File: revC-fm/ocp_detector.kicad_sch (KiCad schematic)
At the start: 13 parts, among them Q5 MMDT3946, Q59 BSZ180, U34 INA300AIDSQT

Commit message: updated fab files
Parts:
- C146: Manufacturer (none) -> TDK; Mfr. Part No (none) -> CGA2B3X7R1H104K050BE
- C71: renamed from C111; Manufacturer (none) -> TDK; Mfr. Part No (none) -> CGA3E1X7R1V105K080AE
- D8: renamed from D20; Manufacturer (none) -> onsemi; Mfr. Part No (none) -> 1SS400T1G
- Q5: Manufacturer (none) -> Diodes Incorporated
- Q59: Manufacturer (none) -> Infineon
- R129: renamed from R224; Manufacturer (none) -> Panasonic; Mfr. Part No (none) -> ERJ-2GEJ102X
- R130: renamed from R223; Manufacturer (none) -> Stackpole Electronics; Mfr. Part No (none) -> RMCF0402FT100K
- R131: renamed from R221; Manufacturer (none) -> Stackpole Electronics; Mfr. Part No (none) -> RMCF0402FT10K0
- R132: renamed from R225; Manufacturer (none) -> Stackpole Electronics; Mfr. Part No (none) -> RMCF0402FT100K
- R133: renamed from R222; Manufacturer (none) -> Panasonic; Mfr. Part No (none) -> ERJ-2GEJ102X
- R36: Manufacturer (none) -> Vishay Dale; Mfr. Part No WSLPx -> WSLP1206R0220
- RN5: renamed from RN7; Manufacturer (none) -> Stackpole Electronics
- U18: renamed from U34; Manufacturer (none) -> Vishay Siliconix

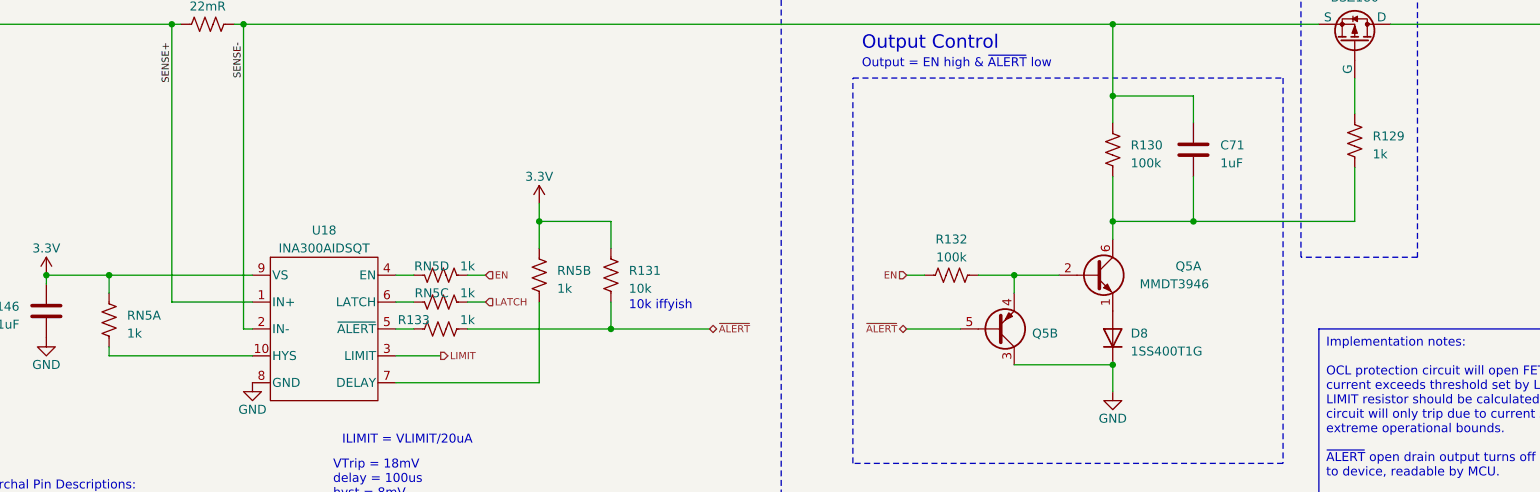
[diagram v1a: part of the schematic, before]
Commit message: updated per review, improved docs
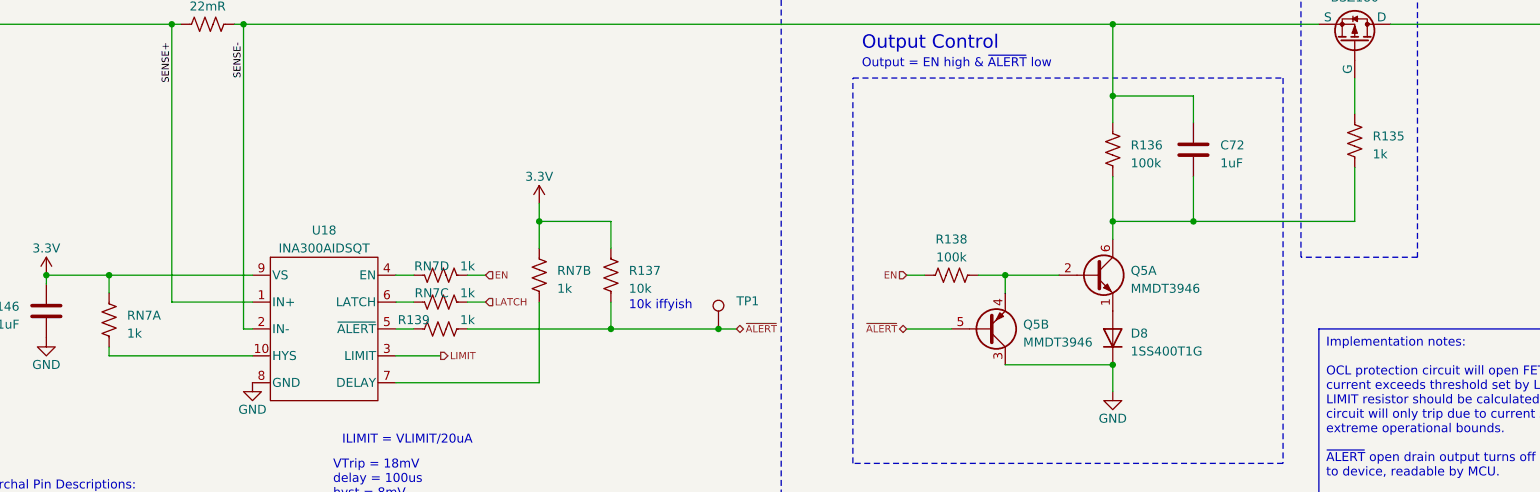
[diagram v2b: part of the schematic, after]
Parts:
- added TP1: RCU-0C, SierraLobo:TestPoint_TE_RCU_0603, symbol Connector:TestPoint
- renumbered C71 to C72, R129 to R135, R130 to R136, R131 to R137, R132 to R138, R133 to R139, RN5 to RN7
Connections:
- net ~{ALERT}: now also TP1.1
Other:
- moved on the sheet: Q5B
